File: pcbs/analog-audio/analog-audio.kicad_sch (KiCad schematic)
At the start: 50 parts, among them J1 AudioJack5, J2 24VDC, J3 VOL, J4 VOL, J5 BASS, J6 TREBLE, J7 Channel, Q1 TIP31, Q2 TIP31, Q3 TIP32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

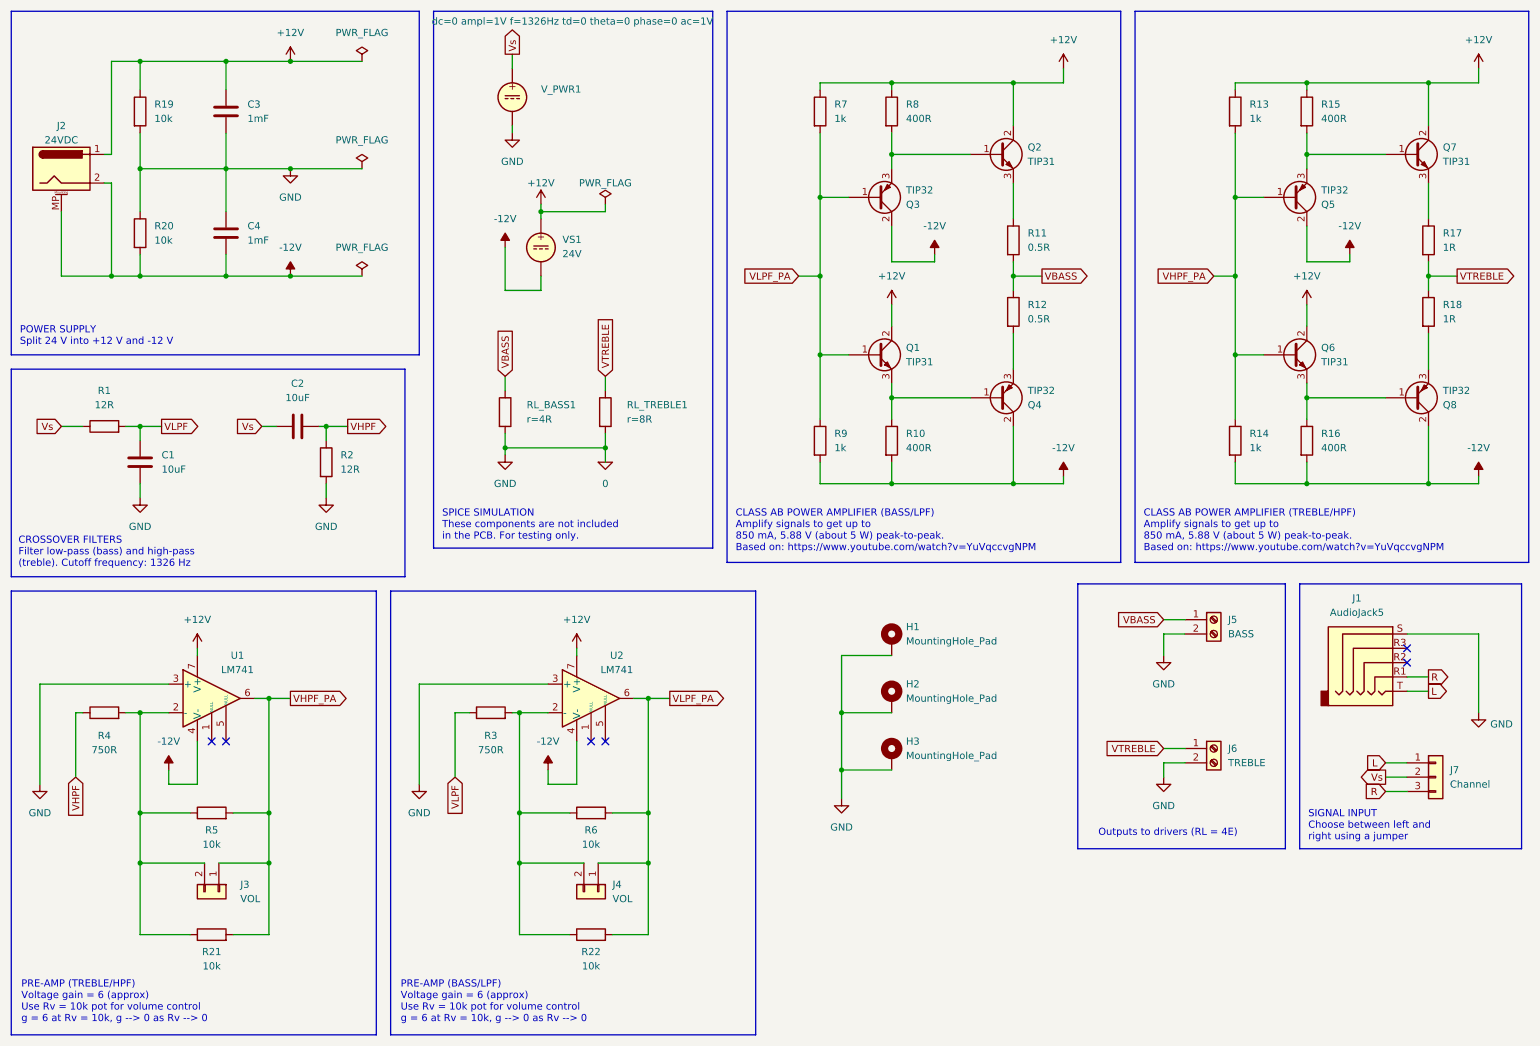
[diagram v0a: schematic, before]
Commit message: fixed error in PCB and updated to use real values
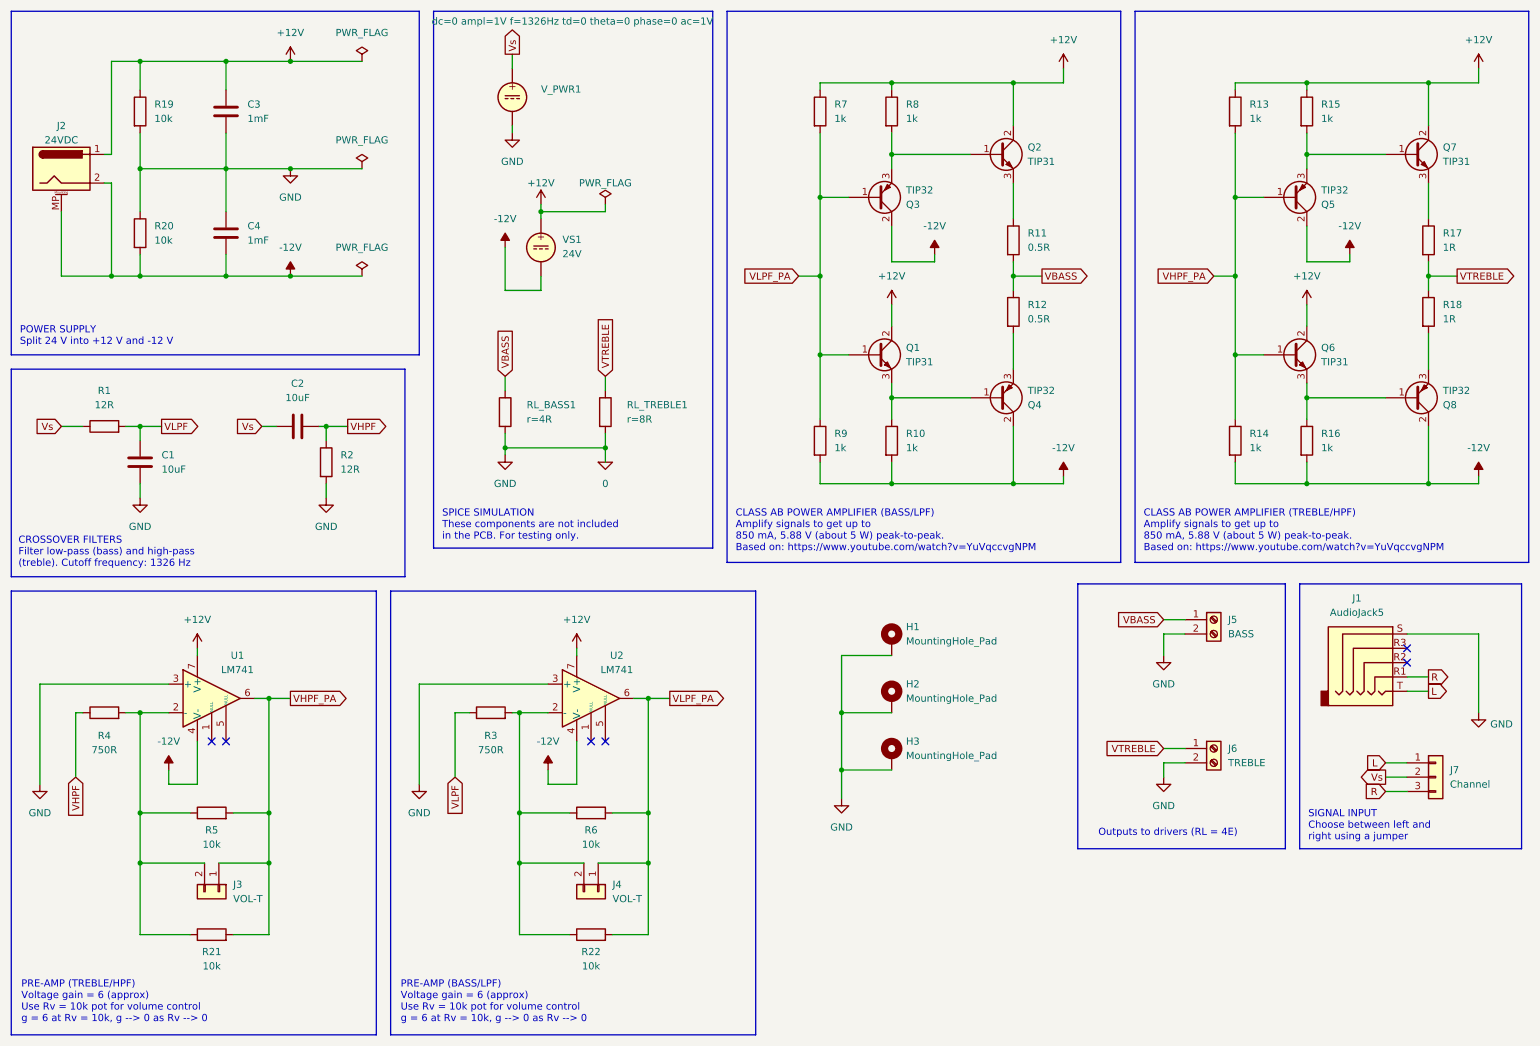
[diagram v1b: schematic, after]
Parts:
- J3, J4: value VOL -> VOL-T
- R10, R15, R16, R8: value 400R -> 1k
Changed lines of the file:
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@@
 		(fields_autoplaced yes)
 		(property "Reference" "J3"
-			(at 54.61 168.9099 90)
-			(effects
-				(font
-					(size 1.27 1.27)
-				)
-				(justify left)
-			)
-		)
-		(property "Value" "VOL"
-			(at 54.61 171.4499 90)
+			(at 53.34 168.9099 90)
+			(effects
+				(font
+					(size 1.27 1.27)
+				)
+				(justify left)
+			)
+		)
+		(property "Value" "VOL-T"
+			(at 53.34 171.4499 90)
 			(effects
 				(font
@@
 			)
 		)
-		(property "Value" "400R"
+		(property "Value" "1k"
 			(at 172.72 91.4399 0)
 			(effects
@@
 			)
 		)
-		(property "Value" "VOL"
+		(property "Value" "VOL-T"
 			(at 120.65 171.4499 90)
 			(effects
@@
 			)
 		)
-		(property "Value" "400R"
+		(property "Value" "1k"
 			(at 246.38 33.0199 0)
 			(effects
@@
 			)
 		)
-		(property "Value" "400R"
+		(property "Value" "1k"
 			(at 246.38 91.4399 0)
 			(effects
@@
 			)
 		)
-		(property "Value" "400R"
+		(property "Value" "1k"
 			(at 172.72 33.0199 0)
 			(effects
